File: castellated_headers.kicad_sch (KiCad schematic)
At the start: 4 parts, among them J5 Conn_01x22, J7 Conn_01x22, J8 Conn_01x22, J9 Conn_01x22

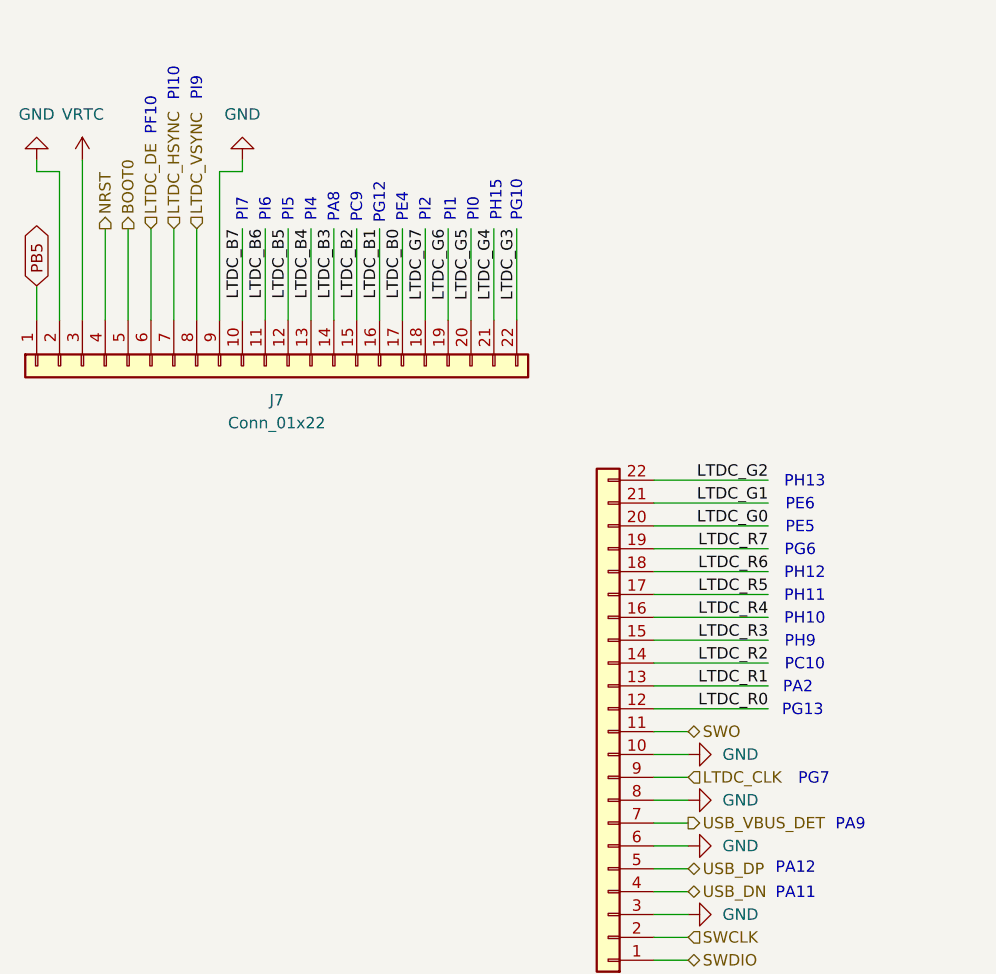
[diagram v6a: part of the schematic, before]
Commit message: Change LCD CLK, VSYNC, HSYNC, to be match with the position of standard 40 pin LCD module
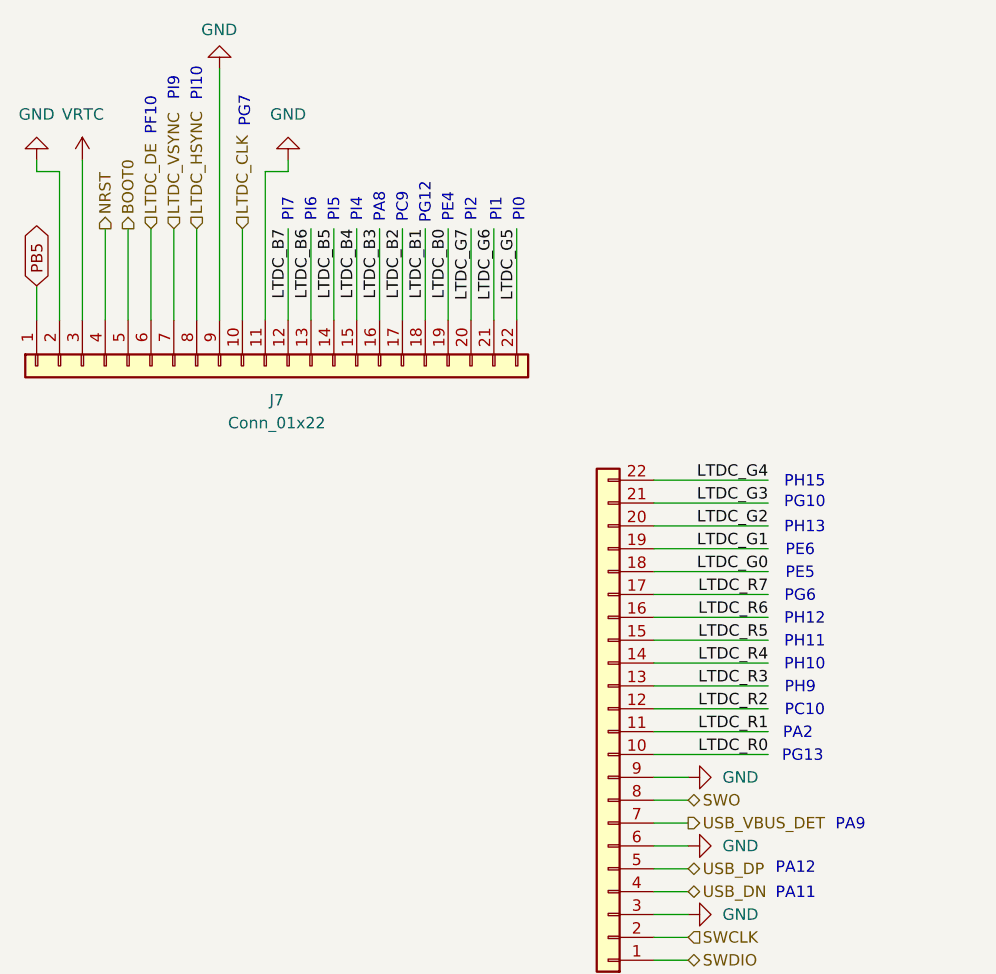
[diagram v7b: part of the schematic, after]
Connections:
- net GND: now also J5.9 (Pin_9), J7.11 (Pin_11); no longer J5.10 (Pin_10), J5.8 (Pin_8)
- net LTDC_B0: now also J7.19 (Pin_19); no longer J7.17 (Pin_17)
- net LTDC_B1: now also J7.18 (Pin_18); no longer J7.16 (Pin_16)
- net LTDC_B2: now also J7.17 (Pin_17); no longer J7.15 (Pin_15)
- net LTDC_B3: now also J7.16 (Pin_16); no longer J7.14 (Pin_14)
- net LTDC_B4: now also J7.15 (Pin_15); no longer J7.13 (Pin_13)
- net LTDC_B5: now also J7.14 (Pin_14); no longer J7.12 (Pin_12)
- net LTDC_B6: now also J7.13 (Pin_13); no longer J7.11 (Pin_11)
- net LTDC_B7: now also J7.12 (Pin_12); no longer J7.10 (Pin_10)
- net LTDC_CLK: now also J7.10 (Pin_10); no longer J5.9 (Pin_9)
- net LTDC_G0: now also J5.18 (Pin_18); no longer J5.20 (Pin_20)
- net LTDC_G1: now also J5.19 (Pin_19); no longer J5.21 (Pin_21)
- net LTDC_G2: now also J5.20 (Pin_20); no longer J5.22 (Pin_22)
- net LTDC_G3: now also J5.21 (Pin_21); no longer J7.22 (Pin_22)
- net LTDC_G4: now also J5.22 (Pin_22); no longer J7.21 (Pin_21)
- net LTDC_G5: now also J7.22 (Pin_22); no longer J7.20 (Pin_20)
- net LTDC_G6: now also J7.21 (Pin_21); no longer J7.19 (Pin_19)
- net LTDC_G7: now also J7.20 (Pin_20); no longer J7.18 (Pin_18)
- net LTDC_HSYNC: now also J7.8 (Pin_8); no longer J7.7 (Pin_7)
- net LTDC_R0: now also J5.10 (Pin_10); no longer J5.12 (Pin_12)
- net LTDC_R1: now also J5.11 (Pin_11); no longer J5.13 (Pin_13)
- net LTDC_R2: now also J5.12 (Pin_12); no longer J5.14 (Pin_14)
- net LTDC_R3: now also J5.13 (Pin_13); no longer J5.15 (Pin_15)
- net LTDC_R4: now also J5.14 (Pin_14); no longer J5.16 (Pin_16)
- net LTDC_R5: now also J5.15 (Pin_15); no longer J5.17 (Pin_17)
- net LTDC_R6: now also J5.16 (Pin_16); no longer J5.18 (Pin_18)
- net LTDC_R7: now also J5.17 (Pin_17); no longer J5.19 (Pin_19)
- net LTDC_VSYNC: now also J7.7 (Pin_7); no longer J7.8 (Pin_8)
- net SWO: now also J5.8 (Pin_8); no longer J5.11 (Pin_11)
